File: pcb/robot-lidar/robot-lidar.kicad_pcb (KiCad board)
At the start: 2 copper layers, 0 parts

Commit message: add i2c pin + crystal + SWD
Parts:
- added C1: 1 uf, Capacitor_SMD:C_0603_1608Metric, F.Cu at (134.2, 80.0)
- added C10: C, Capacitor_SMD:C_0603_1608Metric, F.Cu at (84.2, 77.5)
- added C11: C, Capacitor_SMD:C_0603_1608Metric, F.Cu at (84.2, 80.0)
- added C12: 1 uf, Capacitor_SMD:C_0603_1608Metric, F.Cu at (84.2, 82.5)
- added C13: 1 uf, Capacitor_SMD:C_0603_1608Metric, F.Cu at (84.2, 85.0)
- added C2: 1uf, Capacitor_SMD:C_0603_1608Metric, F.Cu at (134.2, 82.5)
- added C3: 10 uf, Capacitor_SMD:C_0603_1608Metric, F.Cu at (134.2, 85.0)
- added C4: 1 uf, Capacitor_SMD:C_0603_1608Metric, F.Cu at (114.2, 85.0)
- added C5: 1 uf, Capacitor_SMD:C_0603_1608Metric, F.Cu at (114.2, 87.5)
- added C6: 1 uf, Capacitor_SMD:C_0603_1608Metric, F.Cu at (114.2, 90.0)
- added C7: 1 uf, Capacitor_SMD:C_0603_1608Metric, F.Cu at (114.2, 92.5)
- added C8: 1 uf, Capacitor_SMD:C_0603_1608Metric, F.Cu at (114.2, 95.0)
- added C9: C, Capacitor_SMD:C_0603_1608Metric, F.Cu at (84.2, 74.9)
- added J2: YLIDAR X4, Connector_Hirose:Hirose_DF13-08P-1.25DSA_1x08_P1.25mm_Vertical, F.Cu at (96.2, 55.0)
- added J3: Jack-DC, Connector_BarrelJack:BarrelJack_Horizontal, F.Cu at (139.8, 97.8)
- added R1: R_Small, Resistor_SMD:R_0603_1608Metric, F.Cu at (84.2, 87.5)
- added R2: R_Small, Resistor_SMD:R_0603_1608Metric, F.Cu at (84.2, 90.0)
- added U1: STM32F429VETx, Package_QFP:LQFP-100_14x14mm_P0.5mm, F.Cu at (99.5, 98.9)
- added U2: LM317-3.3_SOT-223, Package_TO_SOT_SMD:SOT-223-3_TabPin2, F.Cu at (143.2, 85.0)
- added U3: MPU-6050, Sensor_Motion:InvenSense_QFN-24_4x4mm_P0.5mm, F.Cu at (89.4, 76.9)

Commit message: add components
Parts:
- added C14: 0.1uF, Capacitor_SMD:C_0603_1608Metric, F.Cu at (94.0, 117.7)
- added C15: 0.1uF, Capacitor_SMD:C_0603_1608Metric, F.Cu at (94.0, 120.2)
- added J1: Conn_ARM_SWD_TagConnect_TC2030, Connector_PinHeader_2.54mm:PinHeader_1x06_P2.54mm_Vertical, F.Cu at (98.3, 118.8)
- added J4: Conn_02x03_Odd_Even, Connector_PinHeader_2.54mm:PinHeader_2x03_P2.54mm_Vertical_SMD, F.Cu at (107.1, 127.5)
- added R3: 10k, Resistor_SMD:R_0603_1608Metric, F.Cu at (94.0, 122.7)
- added R4: 10k, Resistor_SMD:R_0603_1608Metric, F.Cu at (94.0, 125.2)
- added R5: 10k, Resistor_SMD:R_0603_1608Metric, F.Cu at (94.0, 127.7)
- added R6: 10k, Resistor_SMD:R_0603_1608Metric, F.Cu at (94.0, 130.2)
- added R7: 10k, Resistor_SMD:R_0603_1608Metric, F.Cu at (94.0, 132.7)
- added SW1: SW_SPST, Button_Switch_SMD:SW_SPST_CK_RS282G05A3, F.Cu at (106.1, 135.0)
- added Y1: Crystal, Crystal:Crystal_SMD_HC49-SD, F.Cu at (108.0, 119.5)
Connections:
- R1 pad 2: SCL -> I2C_SCL
- R2 pad 2: SDA -> I2C_SDA
- U1 pad 14: unconnected-(U1-NRST-Pad14) -> RESET
- U3 pad 23: SCL -> I2C_SCL
- U3 pad 24: SDA -> I2C_SDA

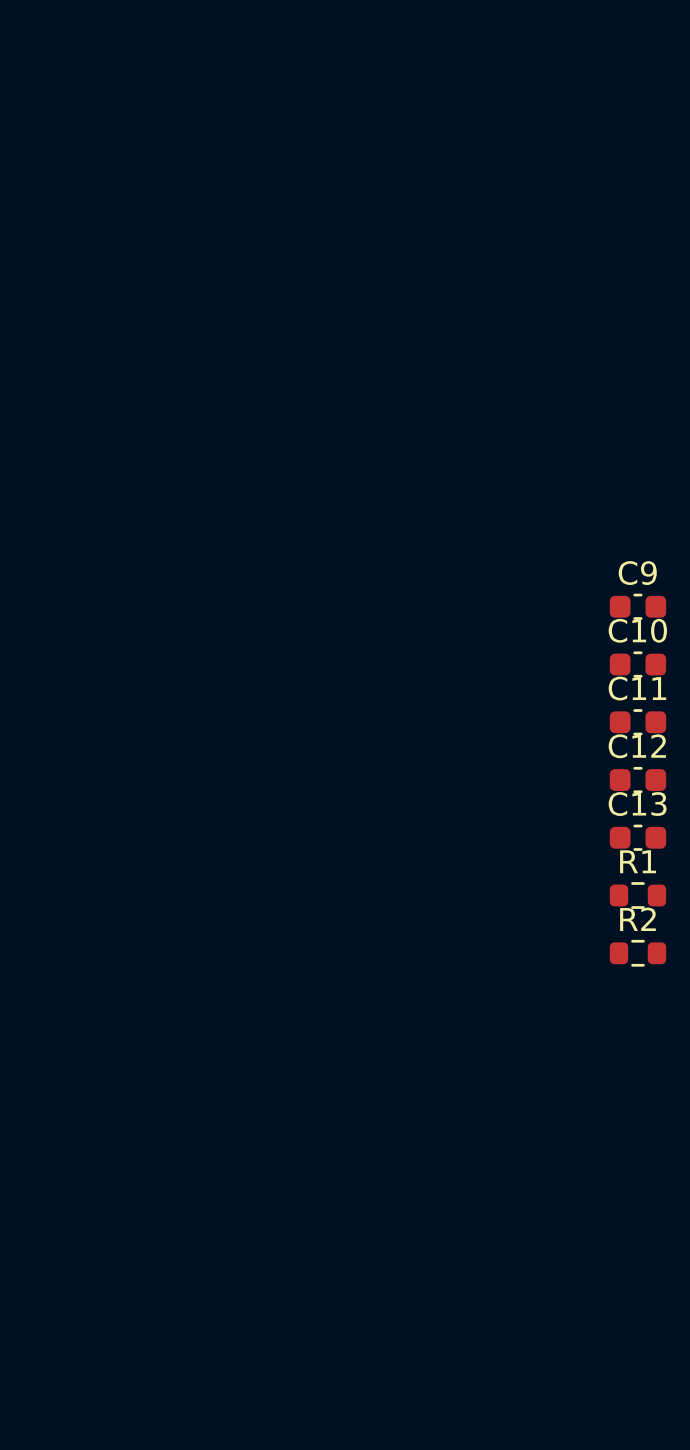
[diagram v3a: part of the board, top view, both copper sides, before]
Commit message: add wiring motor
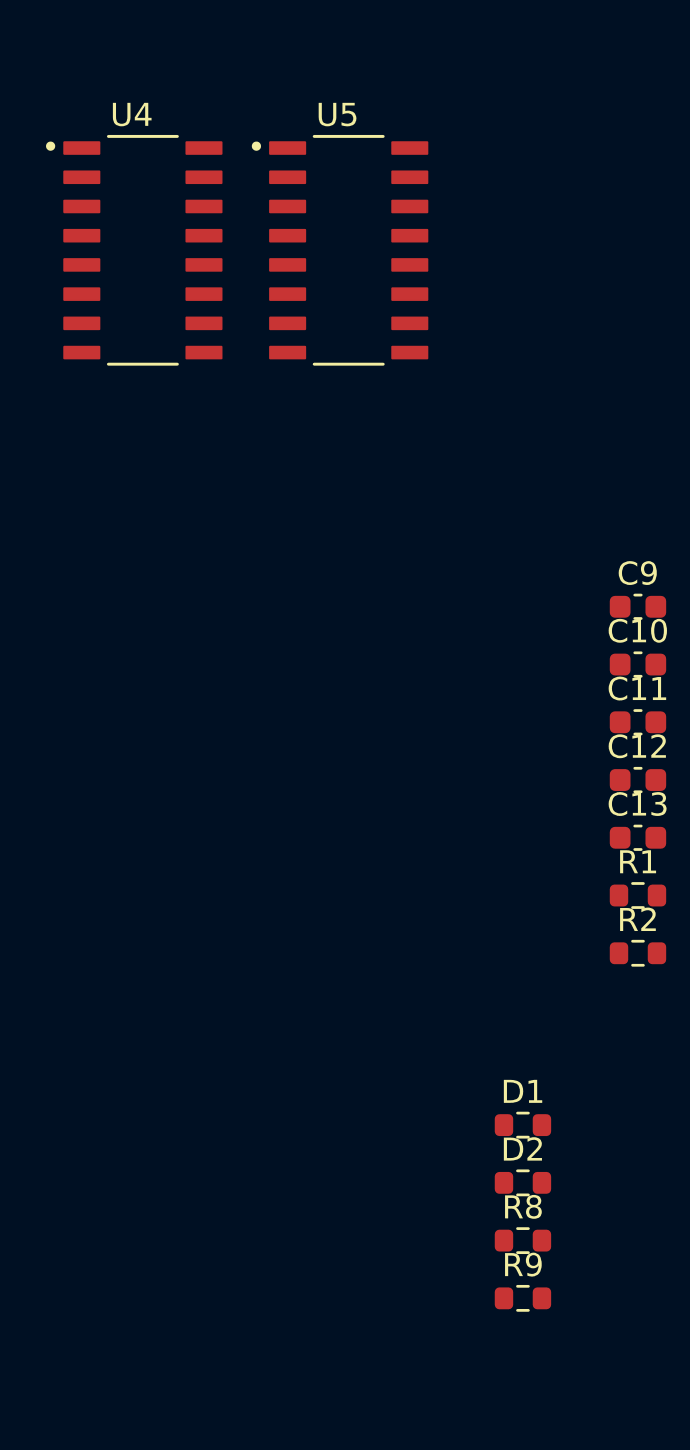
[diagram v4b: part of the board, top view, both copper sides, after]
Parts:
- added D1: LED_Small, Resistor_SMD:R_0603_1608Metric, F.Cu at (79.2, 97.5)
- added D2: LED_Small, Resistor_SMD:R_0603_1608Metric, F.Cu at (79.2, 100.0)
- added R8: 2k, Resistor_SMD:R_0603_1608Metric, F.Cu at (79.2, 102.5)
- added R9: 2k, Resistor_SMD:R_0603_1608Metric, F.Cu at (79.2, 105.0)
- added U4: MX1508, MX1508:SOIC127P600X177-16N, F.Cu at (62.7, 59.4)
- added U5: MX1508, MX1508:SOIC127P600X177-16N, F.Cu at (71.6, 59.4)
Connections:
- U1 pad 12: unconnected-(U1-PH0-Pad12) -> PH0
- U1 pad 13: unconnected-(U1-PH1-Pad13) -> PH1
- U1 pad 23: unconnected-(U1-PA0-Pad23) -> Net-(D1-A)
- U1 pad 24: unconnected-(U1-PA1-Pad24) -> Net-(D2-A)

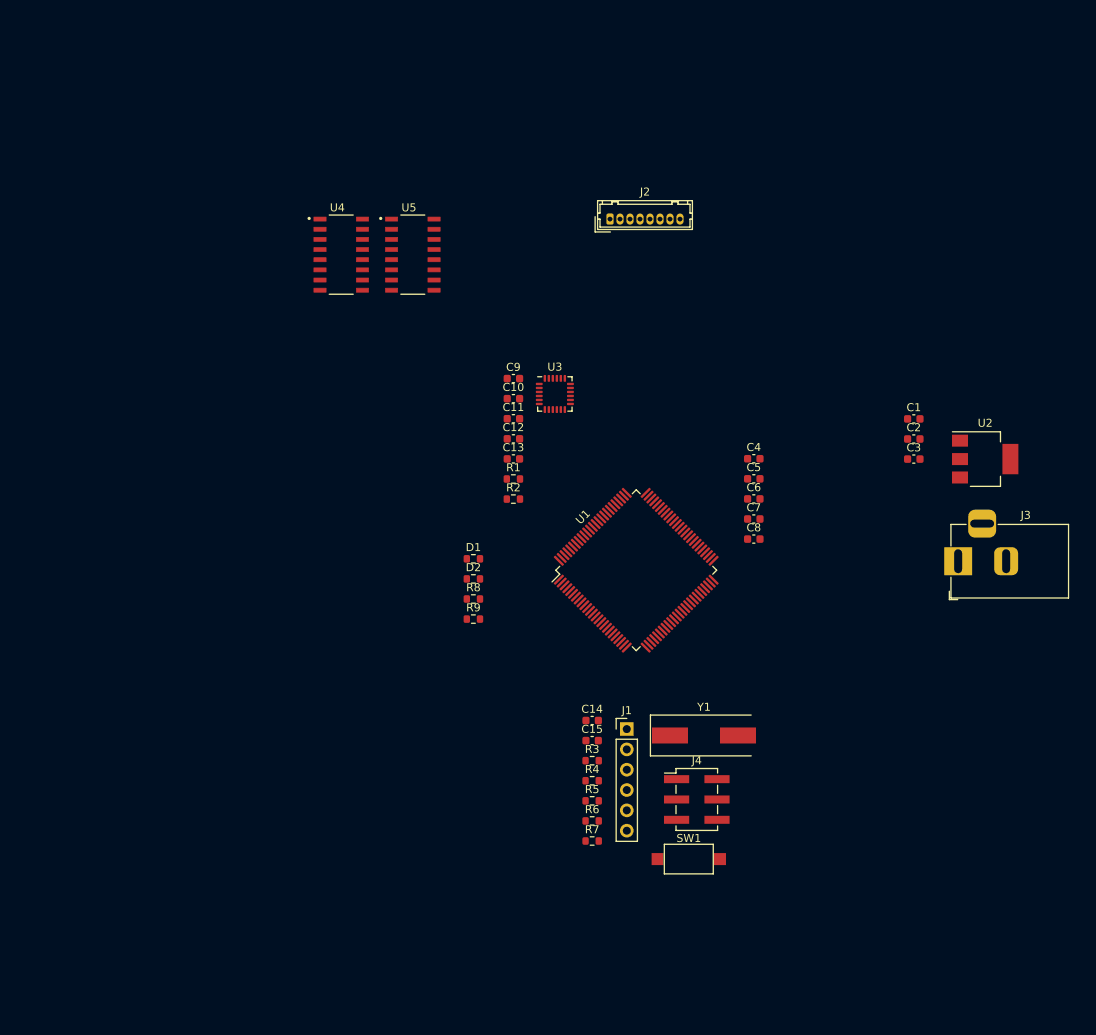
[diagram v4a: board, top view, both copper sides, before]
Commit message: add motor pin
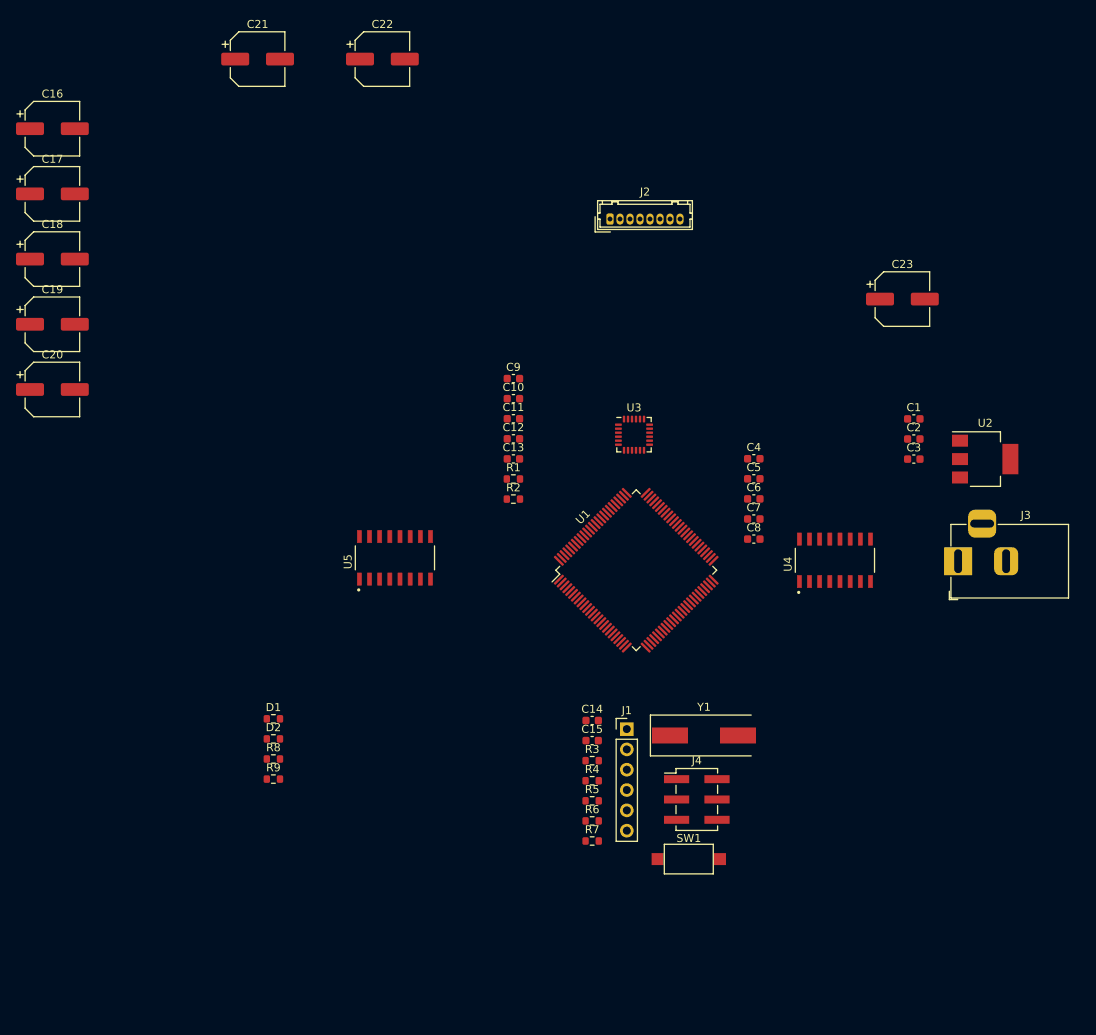
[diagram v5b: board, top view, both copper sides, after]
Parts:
- added C16: C_Polarized_Small, Capacitor_SMD:CP_Elec_6.3x4.9, F.Cu at (26.6, 43.7)
- added C17: C_Polarized_Small, Capacitor_SMD:CP_Elec_6.3x4.9, F.Cu at (26.6, 51.9)
- added C18: C_Polarized_Small, Capacitor_SMD:CP_Elec_6.3x4.9, F.Cu at (26.6, 60.0)
- added C19: C_Polarized_Small, Capacitor_SMD:CP_Elec_6.3x4.9, F.Cu at (26.6, 68.2)
- added C20: C_Polarized_Small, Capacitor_SMD:CP_Elec_6.3x4.9, F.Cu at (26.6, 76.3)
- added C21: C_Polarized_Small, Capacitor_SMD:CP_Elec_6.3x4.9, F.Cu at (52.2, 35.0)
- added C22: C_Polarized_Small, Capacitor_SMD:CP_Elec_6.3x4.9, F.Cu at (67.8, 35.0)
- added C23: C_Polarized_Small, Capacitor_SMD:CP_Elec_6.3x4.9, F.Cu at (132.8, 65.0)
- moved U4 72.6 mm to (124.4, 97.7), turned to 90 degrees
- moved U5 38.0 mm to (69.4, 97.3), turned to 90 degrees
- moved D1 32.0 mm to (54.2, 117.5)
- moved D2 32.0 mm to (54.2, 120.0)
- moved R8 32.0 mm to (54.2, 122.5)
- moved R9 32.0 mm to (54.2, 125.0)
- moved U3 11.1 mm to (99.2, 82.0)
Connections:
- U1 pad 67: unconnected-(U1-PA8-Pad67) -> MOTOR_4_B
- U1 pad 68: unconnected-(U1-PA9-Pad68) -> MOTOR_4_A
- U1 pad 69: unconnected-(U1-PA10-Pad69) -> MOTOR_3_B
- U1 pad 70: unconnected-(U1-PA11-Pad70) -> MOTOR_3_A
- U1 pad 71: unconnected-(U1-PA12-Pad71) -> MOTOR_2_B
- U1 pad 72: unconnected-(U1-PA13-Pad72) -> MOTOR_2_A
- U1 pad 76: unconnected-(U1-PA14-Pad76) -> MOTOR_1_B
- U1 pad 77: unconnected-(U1-PA15-Pad77) -> MOTOR_1_A
- U4 pad 1: unconnected-(U4A-VCC1-Pad1) -> +5V
- U4 pad 10: unconnected-(U4B-AGND2-Pad10) -> GND
- U4 pad 11: unconnected-(U4B-PGND2-Pad11) -> GND
- U4 pad 14: unconnected-(U4A-AGND1-Pad14) -> GND
- U4 pad 15: unconnected-(U4A-PGND1-Pad15) -> GND
- U4 pad 2: unconnected-(U4A-INA1-Pad2) -> MOTOR_1_A
- U4 pad 3: unconnected-(U4A-INB1-Pad3) -> MOTOR_1_B
- U4 pad 4: unconnected-(U4A-VDD1-Pad4) -> +5V
- U4 pad 5: unconnected-(U4B-VCC2-Pad5) -> +5V
- U4 pad 6: unconnected-(U4B-INA2-Pad6) -> MOTOR_2_A
- U4 pad 7: unconnected-(U4B-INB2-Pad7) -> MOTOR_2_B
- U4 pad 8: unconnected-(U4B-VDD2-Pad8) -> +5V
- U5 pad 1: unconnected-(U5A-VCC1-Pad1) -> +5V
- U5 pad 10: unconnected-(U5B-AGND2-Pad10) -> GND
- U5 pad 11: unconnected-(U5B-PGND2-Pad11) -> GND
- U5 pad 14: unconnected-(U5A-AGND1-Pad14) -> GND
- U5 pad 15: unconnected-(U5A-PGND1-Pad15) -> GND
- U5 pad 2: unconnected-(U5A-INA1-Pad2) -> MOTOR_3_A
- U5 pad 3: unconnected-(U5A-INB1-Pad3) -> MOTOR_3_B
- U5 pad 4: unconnected-(U5A-VDD1-Pad4) -> +5V
- U5 pad 5: unconnected-(U5B-VCC2-Pad5) -> +5V
- U5 pad 6: unconnected-(U5B-INA2-Pad6) -> MOTOR_4_A
- U5 pad 7: unconnected-(U5B-INB2-Pad7) -> MOTOR_4_B
- U5 pad 8: unconnected-(U5B-VDD2-Pad8) -> +5V

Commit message: add pcb edge cut
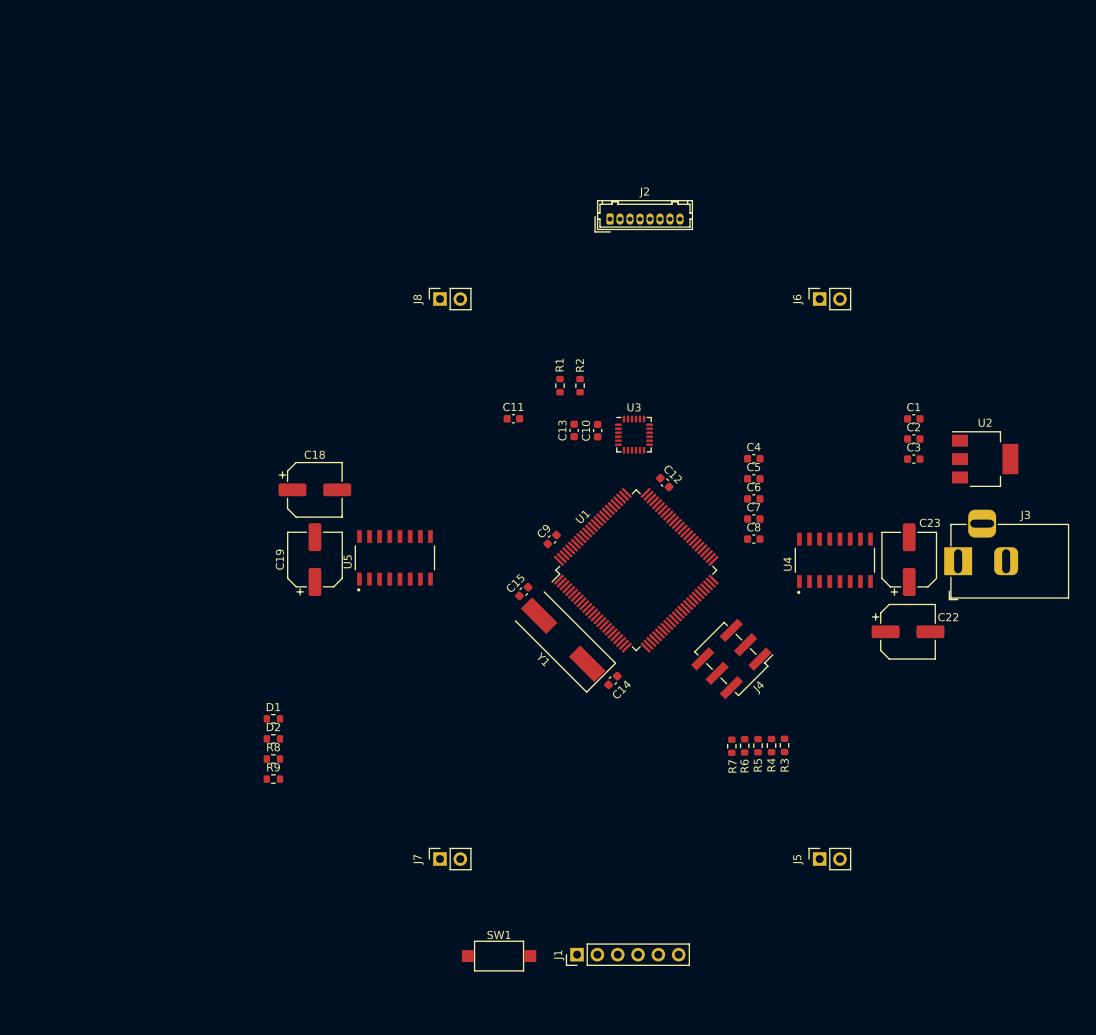
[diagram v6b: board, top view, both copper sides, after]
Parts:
- removed C16, C17, C20, C21: C_Polarized_Small, Capacitor_SMD:CP_Elec_6.3x4.9
- added J5: Conn_01x02, Connector_PinSocket_2.54mm:PinSocket_1x02_P2.54mm_Vertical, F.Cu at (122.5, 135.0)
- added J6: Conn_01x02, Connector_PinSocket_2.54mm:PinSocket_1x02_P2.54mm_Vertical, F.Cu at (122.5, 65.0)
- added J7: Conn_01x02, Connector_PinSocket_2.54mm:PinSocket_1x02_P2.54mm_Vertical, F.Cu at (75.0, 135.0)
- added J8: Conn_01x02, Connector_PinSocket_2.54mm:PinSocket_1x02_P2.54mm_Vertical, F.Cu at (75.0, 65.0)
- moved C22 97.2 mm to (133.5, 106.6)
- moved C19 44.1 mm to (59.4, 97.6), turned to 90 degrees
- moved C18 43.7 mm to (59.4, 88.8)
- moved C23 32.6 mm to (133.7, 97.6), turned to 90 degrees
- moved J1 28.9 mm to (92.1, 146.9), turned to 90 degrees
- moved SW1 26.6 mm to (82.4, 147.1)
- moved R3 24.1 mm to (118.1, 120.8), turned to 90 degrees
- moved R4 22.8 mm to (116.4, 120.8), turned to 90 degrees
- moved R5 21.8 mm to (114.8, 120.8), turned to 90 degrees
- moved Y1 21.3 mm to (90.4, 107.6), turned to 135 degrees
- moved R6 21.3 mm to (113.1, 120.8), turned to 90 degrees
- moved R7 21.1 mm to (111.5, 120.9), turned to 90 degrees
- moved C9 20.7 mm to (89.0, 95.1), turned to 45 degrees
- moved C15 20.5 mm to (85.5, 101.6), turned to 45 degrees
- moved C12 19.7 mm to (103.1, 87.9), turned to -45 degrees
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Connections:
- U4 pad 12: unconnected-(U4B-OUTA2-Pad12) -> Net-(J6-Pin_1)
- U4 pad 13: unconnected-(U4A-OUTB1-Pad13) -> Net-(J5-Pin_2)
- U4 pad 16: unconnected-(U4A-OUTA1-Pad16) -> Net-(J5-Pin_1)
- U4 pad 9: unconnected-(U4B-OUTB2-Pad9) -> Net-(J6-Pin_2)
- U5 pad 12: unconnected-(U5B-OUTA2-Pad12) -> Net-(J8-Pin_1)
- U5 pad 13: unconnected-(U5A-OUTB1-Pad13) -> Net-(J7-Pin_2)
- U5 pad 16: unconnected-(U5A-OUTA1-Pad16) -> Net-(J7-Pin_1)
- U5 pad 9: unconnected-(U5B-OUTB2-Pad9) -> Net-(J8-Pin_2)
